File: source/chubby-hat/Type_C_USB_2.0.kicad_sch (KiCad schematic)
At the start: 10 parts, among them J17 USB_C_Receptacle_USB2.0, Q1 AO3401A, U3 USBLC6-2SC6

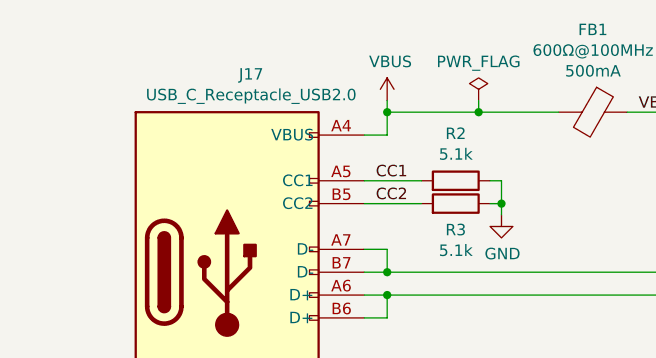
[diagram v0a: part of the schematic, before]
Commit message: added connectors for v8.0; improved power layout
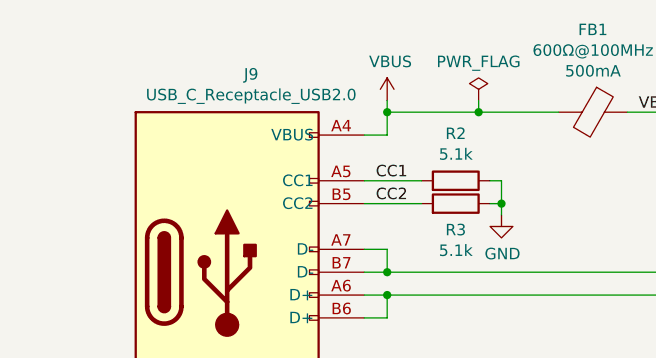
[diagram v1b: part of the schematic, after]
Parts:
- renumbered J17 to J9
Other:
- title: (none) -> ${title}
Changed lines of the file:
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@@
   (paper "A4")
   (title_block
-    (date "2020-08-29")
+    (title "${title}")
+    (date "2023-01-29")
+    (rev "${revision}")
+    (comment 1 "${repo}")
   )
   (junction (at 53.34 43.18) (diameter 0) (color 0 0 0 0)
@@
   (symbol (lib_id "power:GND") (at 99.06 36.83 0) (unit 1)
     (in_bom yes) (on_board yes)
-    (property "Reference" "#PWR056" (id 0) (at 99.06 43.18 0)
+    (property "Reference" "#PWR055" (id 0) (at 99.06 43.18 0)
       (effects (font (size 1.27 1.27)) hide)
     )
@@
   (symbol (lib_id "power:GND") (at 127 53.34 0) (unit 1)
     (in_bom yes) (on_board yes)
-    (property "Reference" "#PWR059" (id 0) (at 127 59.69 0)
+    (property "Reference" "#PWR058" (id 0) (at 127 59.69 0)
       (effects (font (size 1.27 1.27)) hide)
     )
@@
   (symbol (lib_id "Connector:USB_C_Receptacle_USB2.0") (at 35.56 43.18 0) (unit 1)
     (in_bom yes) (on_board yes)
-    (property "Reference" "J17" (id 0) (at 38.227 21.1898 0))
+    (property "Reference" "J9" (id 0) (at 38.227 21.1898 0))
     (property "Value" "USB_C_Receptacle_USB2.0" (id 1) (at 38.227 23.4885 0))
     (property "Footprint" "Connector_USB_Project:USB_C_Receptacle_HRO_TYPE-C-31-D-09" (id 2) (at 39.37 43.18 0)
@@
   (symbol (lib_id "power:+5V") (at 106.68 24.13 0) (unit 1)
     (in_bom yes) (on_board yes)
-    (property "Reference" "#PWR057" (id 0) (at 106.68 27.94 0)
+    (property "Reference" "#PWR056" (id 0) (at 106.68 27.94 0)
       (effects (font (size 1.27 1.27)) hide)
     )
@@
   (symbol (lib_id "power:GND") (at 66.04 36.83 0) (unit 1)
     (in_bom yes) (on_board yes)
-    (property "Reference" "#PWR055" (id 0) (at 66.04 43.18 0)
+    (property "Reference" "#PWR054" (id 0) (at 66.04 43.18 0)
       (effects (font (size 1.27 1.27)) hide)
     )
@@
   (symbol (lib_id "power:VBUS") (at 53.34 24.13 0) (unit 1)
     (in_bom yes) (on_board yes)
-    (property "Reference" "#PWR054" (id 0) (at 53.34 27.94 0)
+    (property "Reference" "#PWR053" (id 0) (at 53.34 27.94 0)
       (effects (font (size 1.27 1.27)) hide)
     )
@@
   (symbol (lib_id "power:VBUS") (at 127 41.91 0) (mirror y) (unit 1)
     (in_bom yes) (on_board yes)
-    (property "Reference" "#PWR058" (id 0) (at 127 45.72 0)
+    (property "Reference" "#PWR057" (id 0) (at 127 45.72 0)
       (effects (font (size 1.27 1.27)) hide)
     )
@@
   (symbol (lib_id "power:GND") (at 157.48 44.45 0) (unit 1)
     (in_bom yes) (on_board yes)
-    (property "Reference" "#PWR060" (id 0) (at 157.48 50.8 0)
+    (property "Reference" "#PWR059" (id 0) (at 157.48 50.8 0)
       (effects (font (size 1.27 1.27)) hide)
     )
@@
   (symbol (lib_id "power:Earth") (at 27.94 77.47 0) (unit 1)
     (in_bom yes) (on_board yes)
-    (property "Reference" "#PWR052" (id 0) (at 27.94 83.82 0)
+    (property "Reference" "#PWR051" (id 0) (at 27.94 83.82 0)
       (effects (font (size 1.27 1.27)) hide)
     )
@@
   (symbol (lib_id "power:GND") (at 38.1 77.47 0) (unit 1)
     (in_bom yes) (on_board yes)
-    (property "Reference" "#PWR053" (id 0) (at 38.1 83.82 0)
-      (effects (font (size 1.27 1.27)) hide)
-    )
+    (property "Reference" "#PWR052" (id 0) (at 38.1 83.82 0)
+      (effects (font (size 1.27 1.27)) hide)
+    )

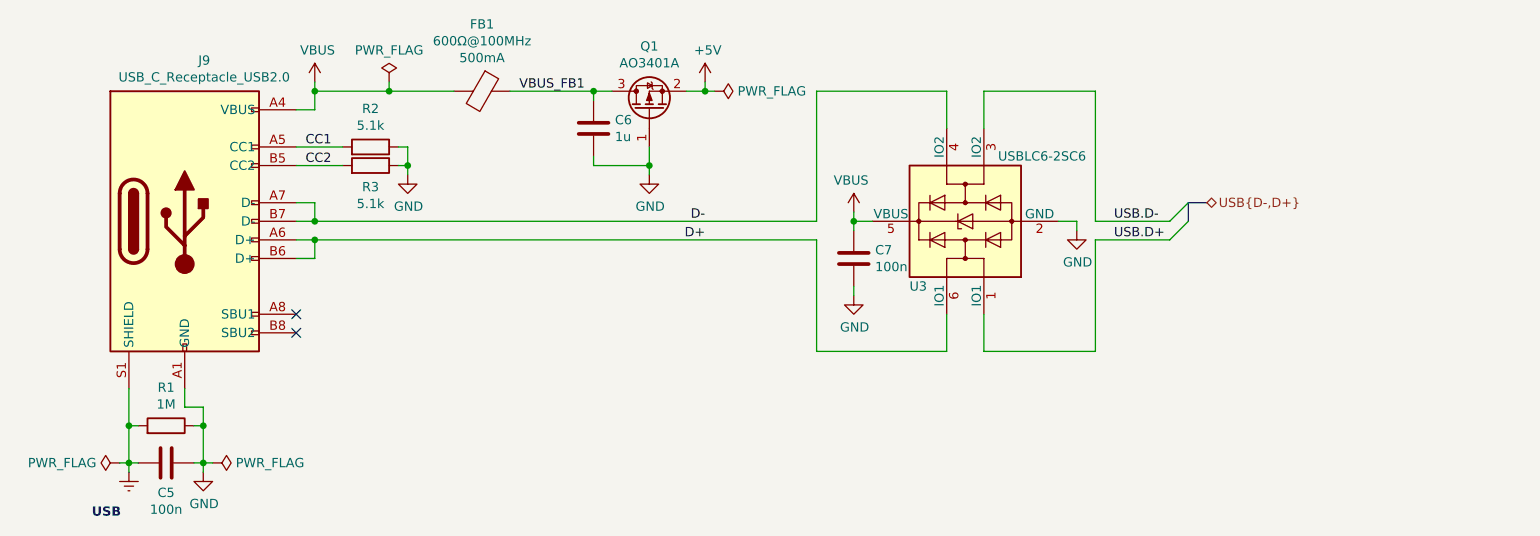
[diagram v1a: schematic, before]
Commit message: add test points and leds - closes #1; add fuse - closes #4; add silk screen art
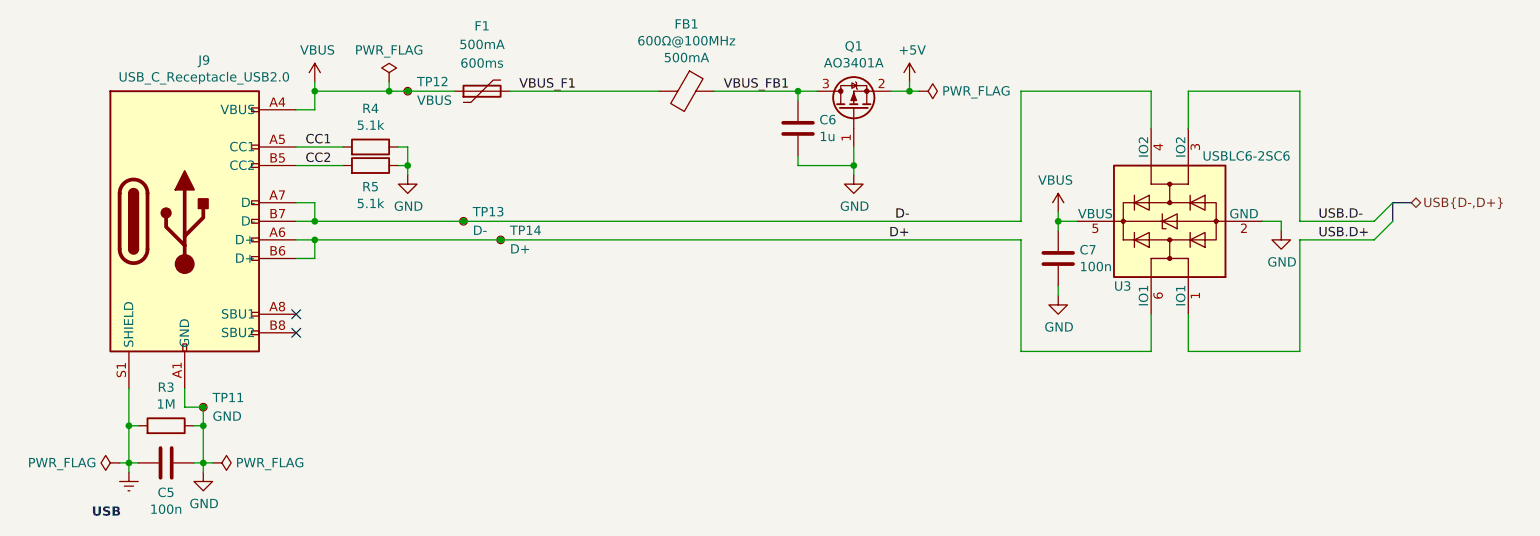
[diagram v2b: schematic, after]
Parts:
- added F1: 500mA, Resistor_SMD:R_0603_1608Metric, symbol Device:Polyfuse
- added TP11: GND, TestPoint:TestPoint_Pad_D1.0mm, symbol Connector:TestPoint_Small
- added TP12: VBUS, TestPoint:TestPoint_Pad_D1.0mm, symbol Connector:TestPoint_Small
- added TP13: D-, TestPoint:TestPoint_Pad_D1.0mm, symbol Connector:TestPoint_Small
- added TP14: D+, TestPoint:TestPoint_Pad_D1.0mm, symbol Connector:TestPoint_Small
- renumbered R1 to R3, R2 to R4, R3 to R5
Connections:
- net D+: now also TP14.1
- net D-: now also TP13.1
- net GND: now also TP11.1
- net VBUS: now also F1.1, TP12.1; no longer FB1.2
- new net VBUS_F1: F1.2, FB1.2
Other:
- moved on the sheet: C6, C7, FB1, Q1, U3

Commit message: add zero volt diodes to USB and modules; add status LEDs; add RP2040 SWD - closes #9
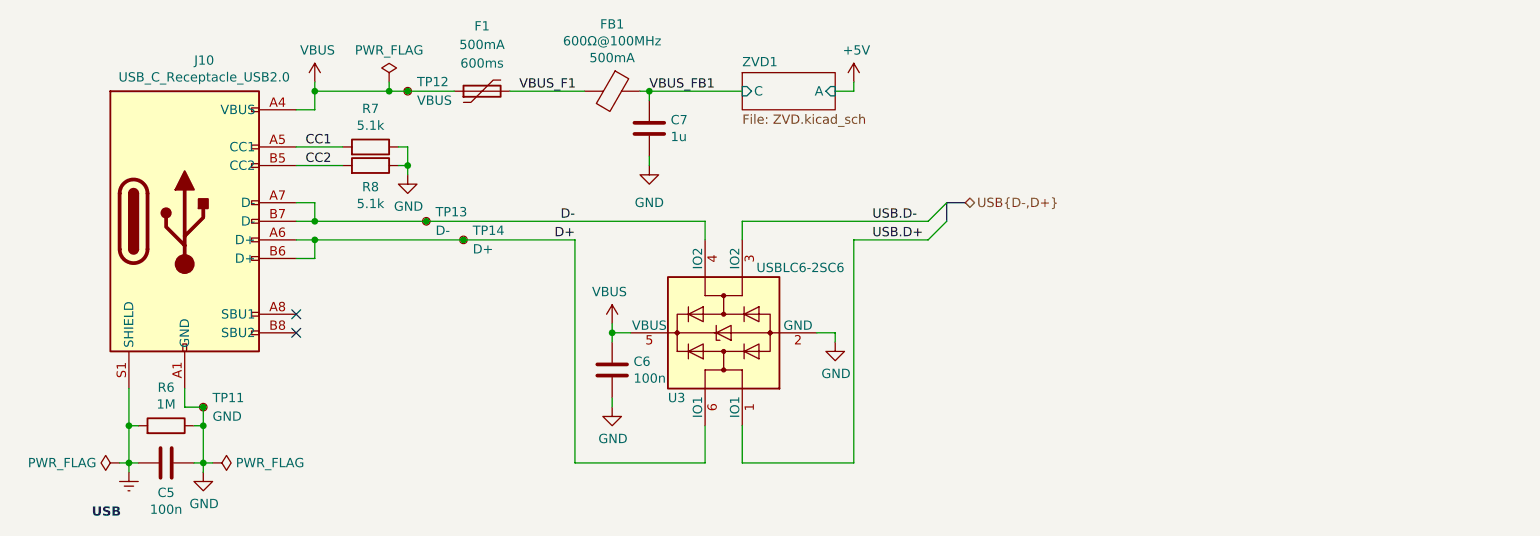
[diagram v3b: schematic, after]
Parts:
- removed Q1: AO3401A, Package_TO_SOT_SMD:SOT-23, symbol Transistor_FET:AO3401A
- renumbered C7 to C6, C6 to C7, J9 to J10, R3 to R6, R4 to R7, R5 to R8
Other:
- added sheet ZVD1 (ZVD.kicad_sch)
- moved on the sheet: C6, C7, FB1, TP13, TP14, U3

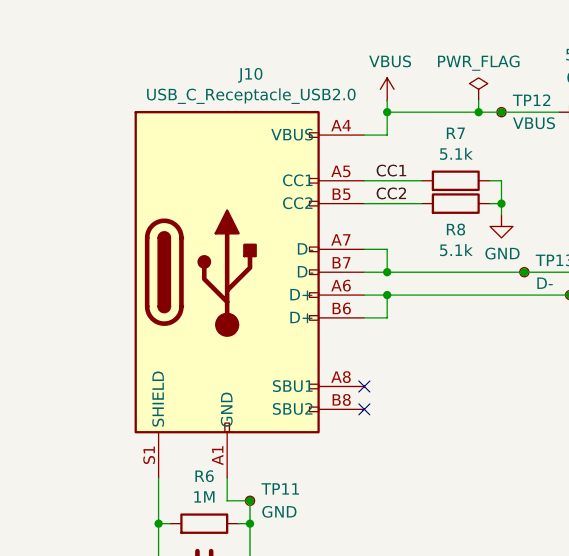
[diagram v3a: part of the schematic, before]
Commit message: moved to KiCad v7.0.0
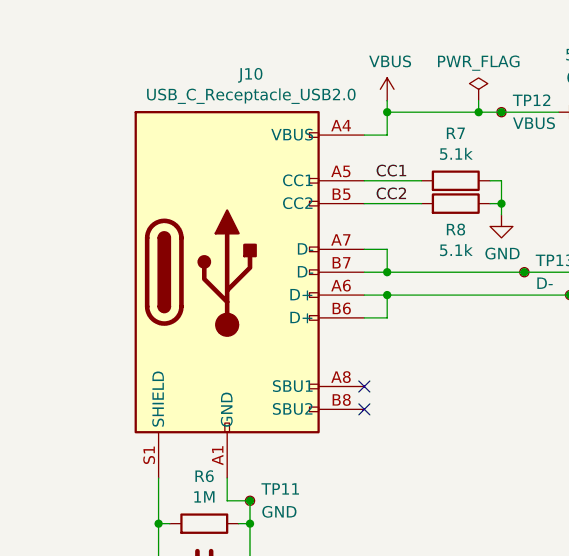
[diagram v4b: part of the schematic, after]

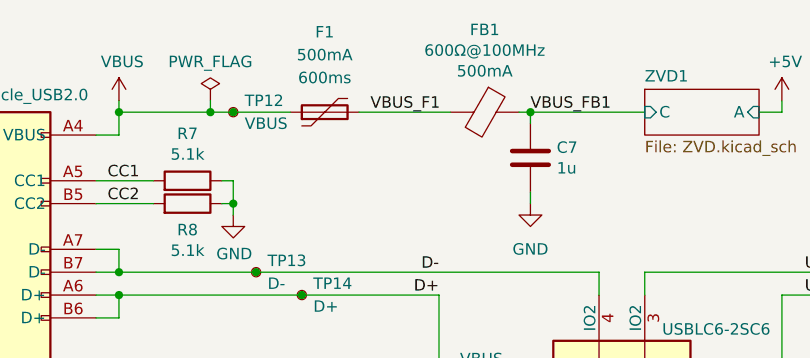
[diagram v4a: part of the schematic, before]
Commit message: add prototyping area; closes #14
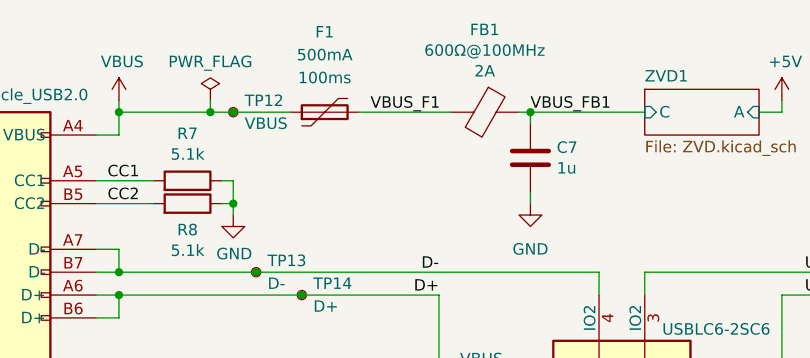
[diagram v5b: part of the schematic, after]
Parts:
- F1: LCSC C261935 -> C914092; MPN TLC-FSMD020 -> BSMD0603-075-6V; T_trip 600ms -> 100ms
- FB1: I_max 500mA -> 2A; LCSC (none) -> C370570; MPN FCM1608KF-601T05 -> UPZ1608E601-2R0TF
- J10: LCSC (none) -> C2848615; MPN (none) -> TYPE-C-31-D-09
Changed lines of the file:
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@@
+      (effects (font (size 1.27 1.27)) hide)
+    )
+    (property "LCSC" "C2848615" (at 35.56 43.18 0)
+      (effects (font (size 1.27 1.27)) hide)
+    )
+    (property "MPN" "TYPE-C-31-D-09" (at 35.56 43.18 0)
       (effects (font (size 1.27 1.27)) hide)
     )
@@
       (effects (font (size 1.27 1.27)) hide)
     )
-    (property "Datasheet" "https://datasheet.lcsc.com/szlcsc/1809192135_TAITEC-FCM1608KF-601T05_C133937.pdf" (at 93.98 25.4 0)
-      (effects (font (size 1.27 1.27)) hide)
-    )
-    (property "MPN" "FCM1608KF-601T05" (at 93.98 25.4 90)
-      (effects (font (size 1.27 1.27)) hide)
-    )
-    (property "I_max" "500mA" (at 93.98 20.847 90)
-      (effects (font (size 1.27 1.27)))
+    (property "Datasheet" "https://www.sunlordinc.com/UploadFiles/PDF_Cat/20110524142806261.pdf" (at 93.98 25.4 0)
+      (effects (font (size 1.27 1.27)) hide)
+    )
+    (property "MPN" "UPZ1608E601-2R0TF" (at 93.98 25.4 90)
+      (effects (font (size 1.27 1.27)) hide)
+    )
+    (property "I_max" "2A" (at 93.98 20.847 90)
+      (effects (font (size 1.27 1.27)))
+    )
+    (property "LCSC" "C370570" (at 93.98 25.4 90)
+      (effects (font (size 1.27 1.27)) hide)
     )
     (pin "1")
@@
       (effects (font (size 1.27 1.27)) hide)
     )
-    (property "MPN" "TLC-FSMD020" (at 76.2 25.4 90)
-      (effects (font (size 1.27 1.27)) hide)
-    )
-    (property "LCSC" "C261935" (at 76.2 25.4 90)
-      (effects (font (size 1.27 1.27)) hide)
-    )
-    (property "T_trip" "600ms" (at 76.2 21.59 90)
-      (effects (font (size 1.27 1.27)))
-    )
+    (property "MPN" "BSMD0603-075-6V" (at 76.2 25.4 90)
+      (effects (font (size 1.27 1.27)) hide)
+    )
+    (property "LCSC" "C914092" (at 76.2 25.4 90)
+      (effects (font (size 1.27 1.27)) hide)
+    )
+    (property "T_trip" "100ms" (at 76.2 21.59 90)
+      (effects (font (size 1.27 1.27)))
+    )
